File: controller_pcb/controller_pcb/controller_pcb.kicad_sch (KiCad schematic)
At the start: 2 parts

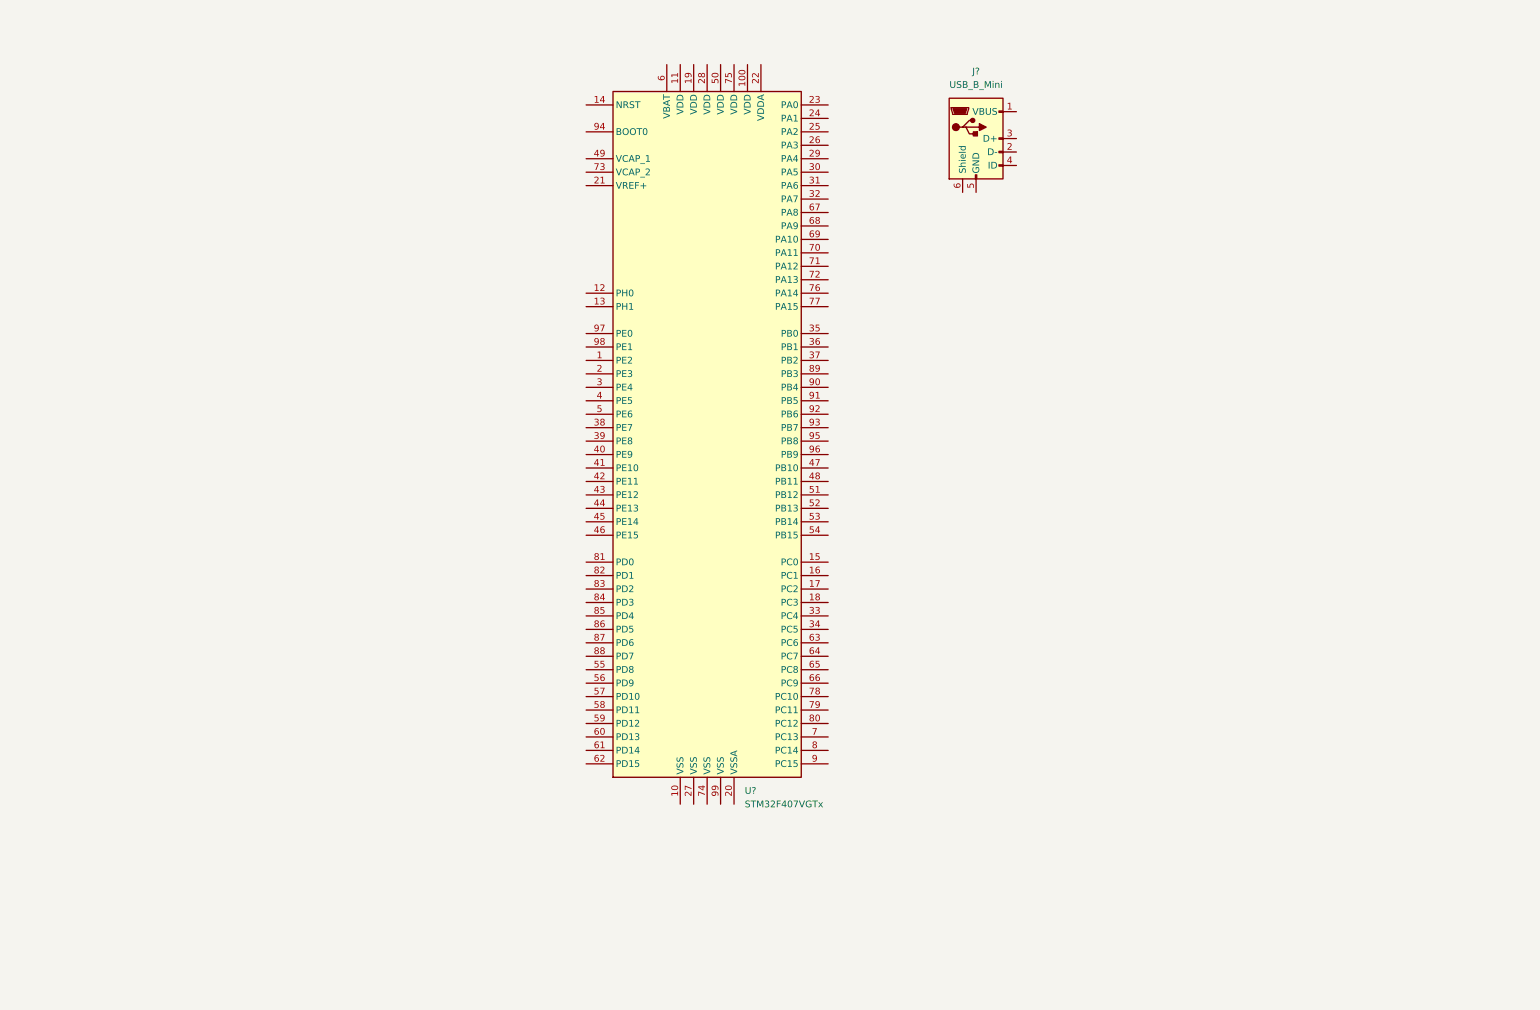
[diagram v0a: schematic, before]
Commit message: Added USB and SW Connector
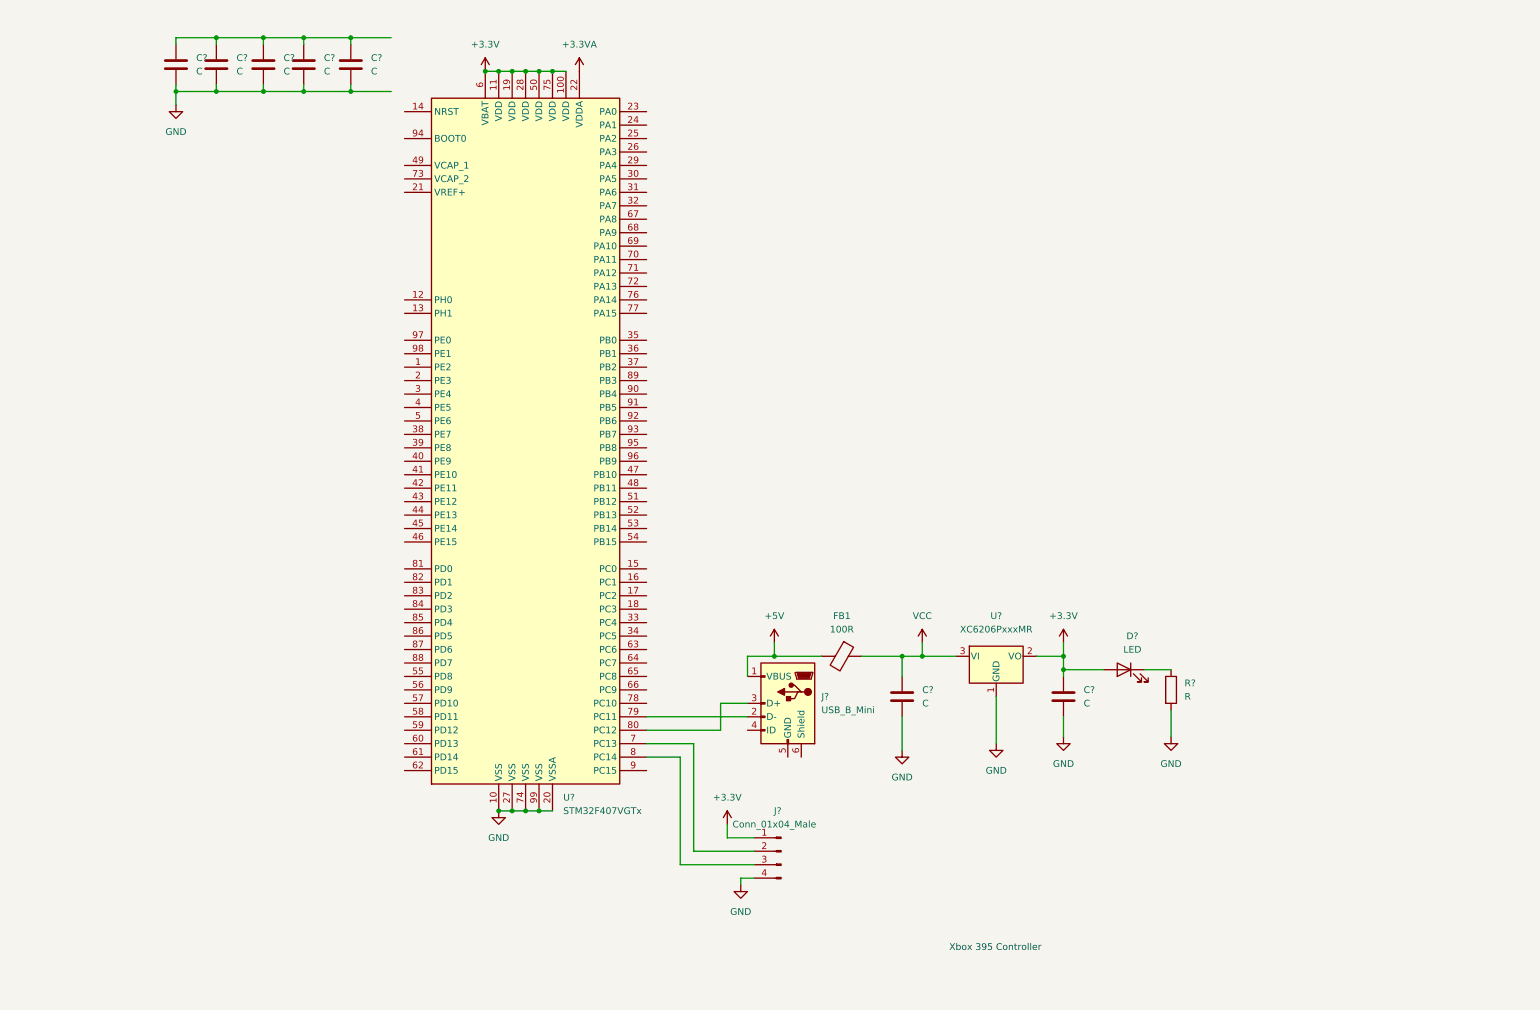
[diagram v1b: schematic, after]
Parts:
- added C? (x7): C, symbol Device:C
- added D?: LED, symbol Device:LED
- added FB1: 100R, symbol Device:FerriteBead
- added J?: Conn_01x04_Male, symbol Connector:Conn_01x04_Male
- added R?: R, symbol Device:R
- added U?: XC6206PxxxMR, Package_TO_SOT_SMD:SOT-23, symbol Regulator_Linear:XC6206PxxxMR
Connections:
- net GND: now reaches U?.10 (VSS)
- net GND: now also U?.20 (VSSA), U?.27 (VSS), U?.74 (VSS), U?.99 (VSS), C?.2, C?.2, C?.2, C?.2, C?.2, C?.2, C?.2, J?.4 (Pin_4), R?.2, U?.1 (GND)
- net +3V3: now reaches U?.100 (VDD)
- net +3V3: now also U?.11 (VDD), U?.19 (VDD), U?.28 (VDD), U?.50 (VDD), U?.6 (VBAT), U?.75 (VDD), C?.1, D?.2 (A), J?.1 (Pin_1), U?.2 (VO)
- net +3.3VA: now reaches U?.22 (VDDA)
- net at U?.7 (PC13): now also J?.2 (Pin_2)
- net at U?.79 (PC11): now also J?.2 (D-)
- net at U?.8 (PC14): now also J?.3 (Pin_3)
- net at U?.80 (PC12): now also J?.3 (D+)
- net +5V: now reaches J?.1 (VBUS)
- net +5V: now also FB1.2
- new net: D?.1 (K), R?.1
- new net: C?.1, C?.1, C?.1, C?.1, C?.1
- new net VCC: C?.1, FB1.1, U?.3 (VI)
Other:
- note added: "Xbox 395 Controller"
- moved on the sheet: J?, U?

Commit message: added one button
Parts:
- added SW?: SW_MEC_5E, symbol Switch:SW_MEC_5E
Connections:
- net GND: now also SW?.3 (K)
- net at U?.17 (PC2): now also SW?.2
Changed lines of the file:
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@@
+    (stroke (width 0) (type default) (color 0 0 0 0))
+  )
+  (wire (pts (xy 148.59 121.92) (xy 148.59 123.19))
     (stroke (width 0) (type default) (color 0 0 0 0))
   )
@@
     (stroke (width 0) (type default) (color 0 0 0 0))
   )
+  (wire (pts (xy 130.81 123.19) (xy 135.89 123.19))
+    (stroke (width 0) (type default) (color 0 0 0 0))
+  )
   (wire (pts (xy 58.42 27.94) (xy 66.04 27.94))
     (stroke (width 0) (type default) (color 0 0 0 0))
@@
     (stroke (width 0) (type default) (color 0 0 0 0))
   )
+  (wire (pts (xy 135.89 123.19) (xy 135.89 121.92))
+    (stroke (width 0) (type default) (color 0 0 0 0))
+  )
   (wire (pts (xy 179.07 134.62) (xy 182.88 134.62))
     (stroke (width 0) (type default) (color 0 0 0 0))
@@
   )
   (wire (pts (xy 58.42 17.78) (xy 66.04 17.78))
+    (stroke (width 0) (type default) (color 0 0 0 0))
+  )
+  (wire (pts (xy 146.05 121.92) (xy 148.59 121.92))
     (stroke (width 0) (type default) (color 0 0 0 0))
   )
@@
     (pin "1")
     (pin "2")
+  )
+  (symbol (lib_id "power:GND") (at 148.59 123.19 0) (unit 1)
+    (in_bom yes) (on_board yes) (fields_autoplaced)
+    (property "Reference" "#PWR?" (id 0) (at 148.59 129.54 0)
+      (effects (font (size 1.27 1.27)) hide)
+    )
+    (property "Value" "GND" (id 1) (at 148.59 128.27 0))
+    (property "Footprint" "" (id 2) (at 148.59 123.19 0)
+      (effects (font (size 1.27 1.27)) hide)
+    )
+    (property "Datasheet" "" (id 3) (at 148.59 123.19 0)
+      (effects (font (size 1.27 1.27)) hide)
+    )
+    (pin "1")
   )
   (symbol (lib_id "power:+3.3V") (at 100.33 24.13 0) (unit 1)
@@
     (pin "2")
   )
+  (symbol (lib_id "Switch:SW_MEC_5E") (at 140.97 121.92 0) (unit 1)
+    (in_bom yes) (on_board yes) (fields_autoplaced)
+    (property "Reference" "SW?" (id 0) (at 140.97 111.76 0))
+    (property "Value" "SW_MEC_5E" (id 1) (at 140.97 114.3 0))
+    (property "Footprint" "" (id 2) (at 140.97 114.3 0)
+      (effects (font (size 1.27 1.27)) hide)
+    )
+    (property "Datasheet" "http://www.apem.com/int/index.php?controller=attachment&id_attachment=1371" (id 3) (at 140.97 114.3 0)
+      (effects (font (size 1.27 1.27)) hide)
+    )
+    (pin "1")
+    (pin "2")
+    (pin "3")
+    (pin "4")
+  )
   (symbol (lib_id "power:GND") (at 148.59 177.8 0) (unit 1)
     (in_bom yes) (on_board yes) (fields_autoplaced)
@@
       (reference "#PWR?") (unit 1) (value "+3.3V") (footprint "")
     )
+    (path "/258bb5a8-c0f3-4b9a-b48a-8d07cffbd7e2"
+      (reference "#PWR?") (unit 1) (value "GND") (footprint "")
+    )
     (path "/261434a5-b86f-484c-94ef-3e941aaa290e"
       (reference "#PWR?") (unit 1) (value "+3.3V") (footprint "")
@@
       (reference "R?") (unit 1) (value "R") (footprint "")
     )
+    (path "/adaa39b1-4a83-435a-8ed8-680108ecec0f"
+      (reference "SW?") (unit 1) (value "SW_MEC_5E") (footprint "")
+    )
     (path "/3a1c998c-e2a1-4320-ae03-3251637afe67"

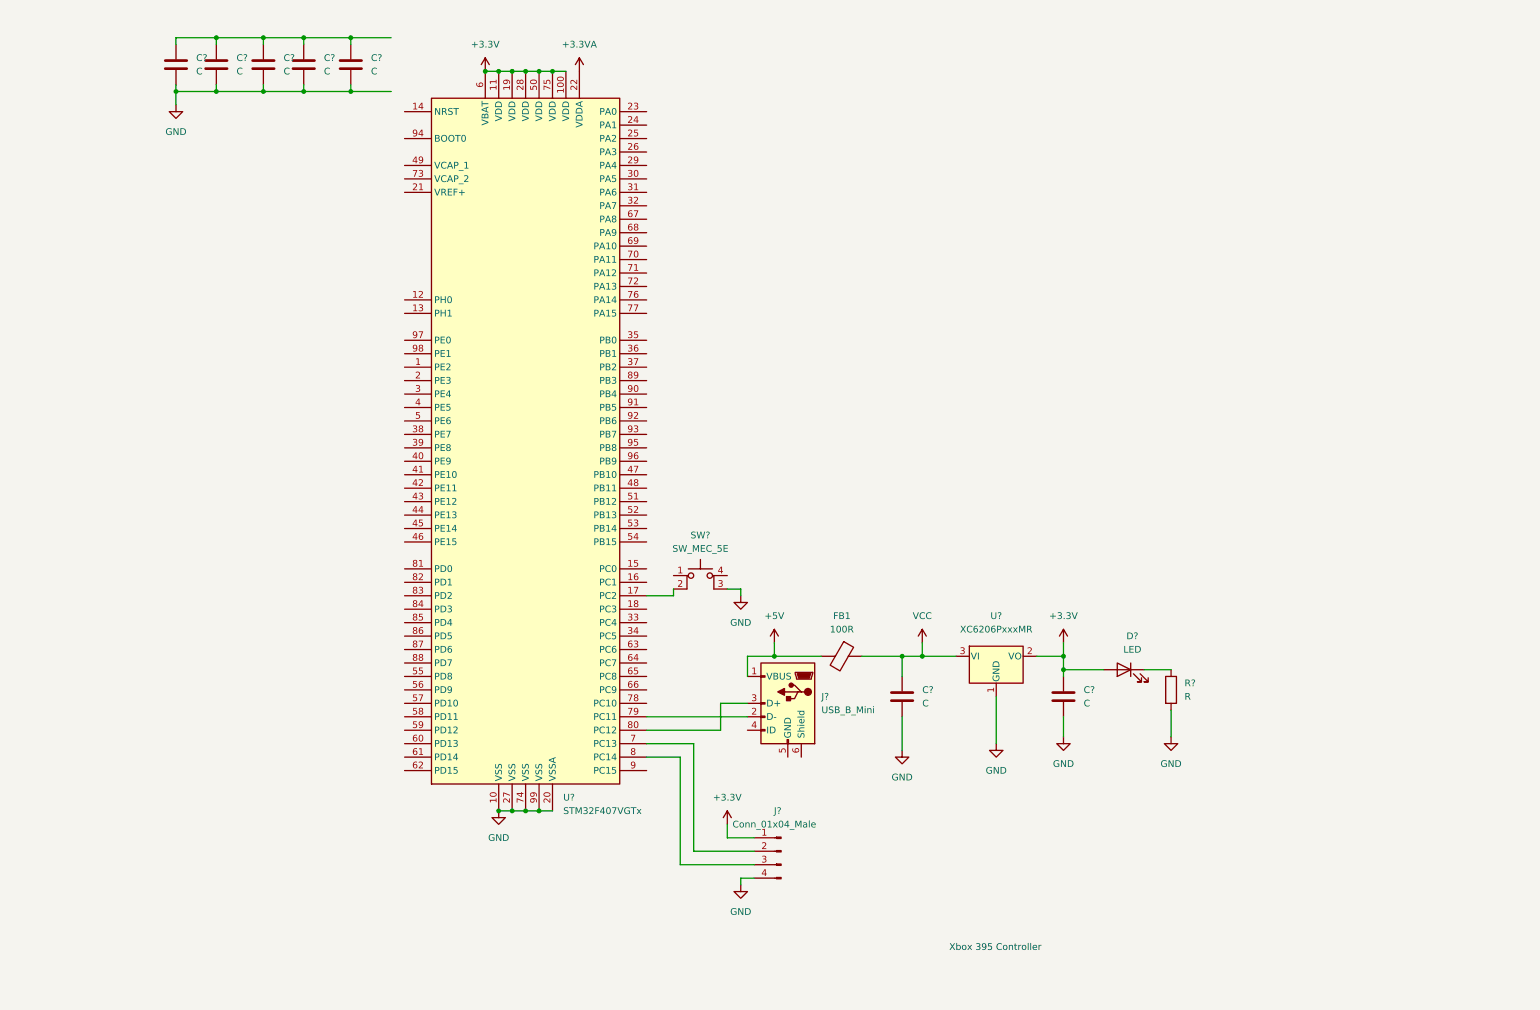
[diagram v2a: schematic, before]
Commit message: added all but one buttons
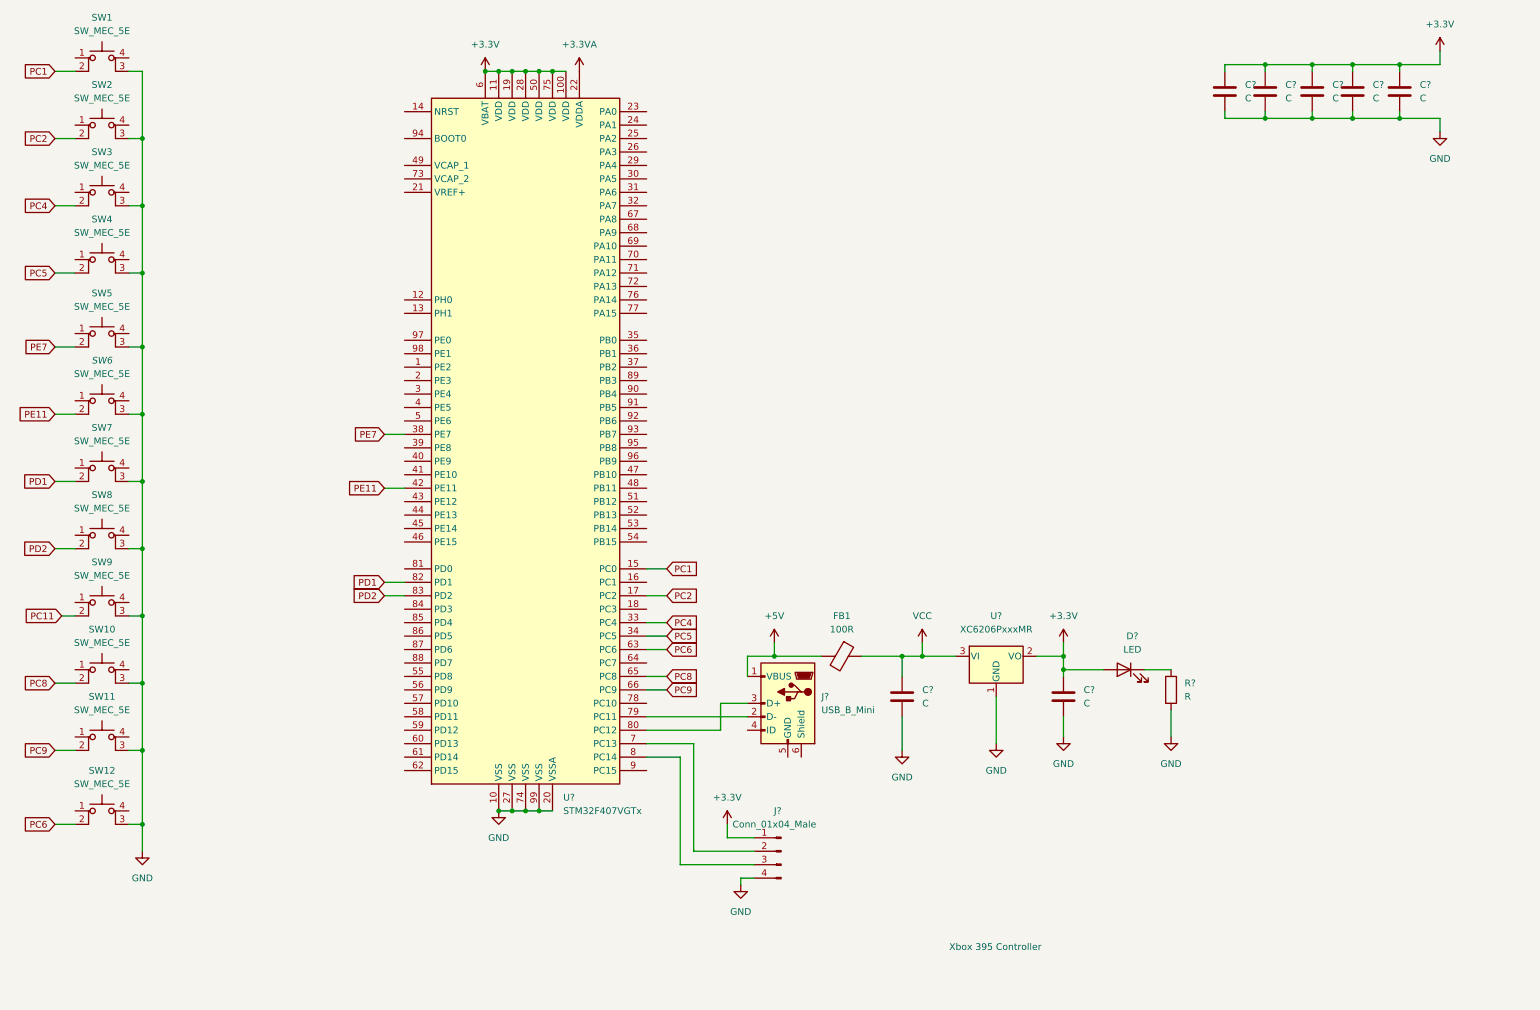
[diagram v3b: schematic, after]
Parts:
- added SW10, SW11, SW12, SW2, SW3, SW4, SW5, SW6, SW7, SW8, SW9: SW_MEC_5E, symbol Switch:SW_MEC_5E
- gave numbers to parts that had none: 1
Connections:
- net +3V3: now also C?.1, C?.1, C?.1, C?.1, C?.1
- net GND: now also SW10.3 (K), SW11.3 (K), SW12.3 (K), SW2.3 (K), SW3.3 (K), SW4.3 (K), SW5.3 (K), SW6.3 (K), SW7.3 (K), SW8.3 (K), SW9.3 (K)
- net PC1: now reaches U?.15 (PC0)
- net PC1: now also SW1.2
- net PC2: now reaches U?.17 (PC2)
- net PC2: now also SW2.2; no longer SW1.2
- net PC4: now reaches U?.33 (PC4)
- net PC4: now also SW3.2
- net PC5: now reaches U?.34 (PC5)
- net PC5: now also SW4.2
- net PE7: now reaches U?.38 (PE7)
- net PE7: now also SW5.2
- net PE11: now reaches U?.42 (PE11)
- net PE11: now also SW6.2
- net PC6: now reaches U?.63 (PC6)
- net PC6: now also SW12.2
- net PC8: now reaches U?.65 (PC8)
- net PC8: now also SW10.2
- net PC9: now reaches U?.66 (PC9)
- net PC9: now also SW11.2
- net PD1: now reaches U?.82 (PD1)
- net PD1: now also SW7.2
- net PD2: now reaches U?.83 (PD2)
- net PD2: now also SW8.2
- new net PC11: SW9.2
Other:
- moved on the sheet: C?, SW1

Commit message: changed port assignments
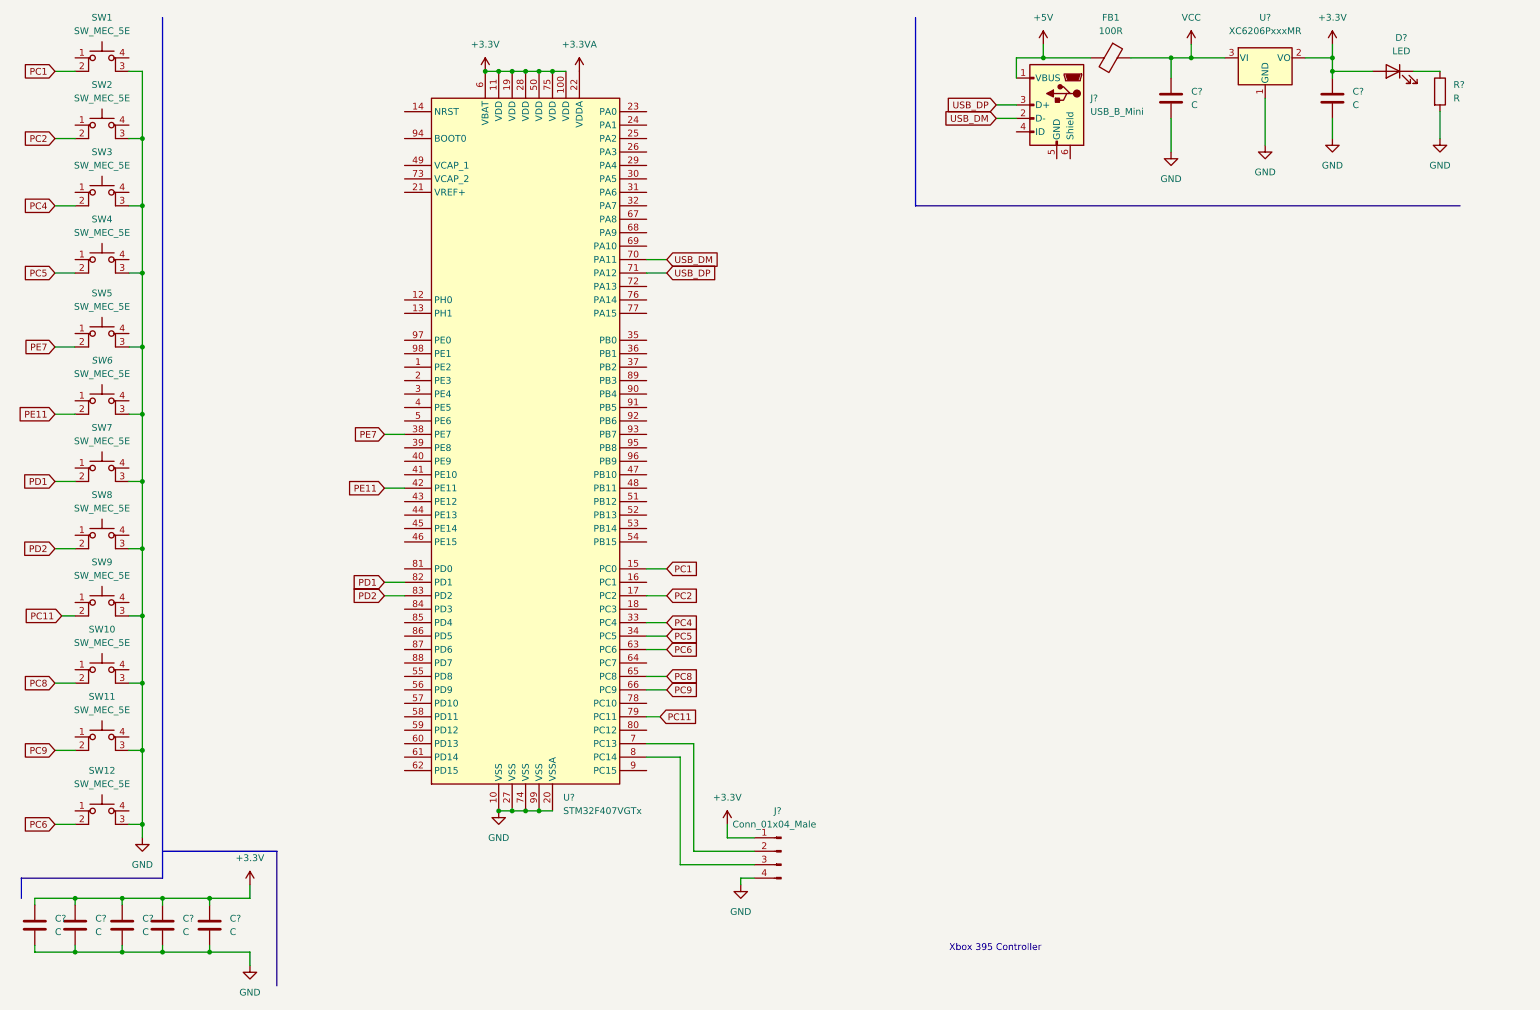
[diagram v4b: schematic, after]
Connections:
- net PC11: now also U?.79 (PC11)
- net USB_DM: now reaches U?.70 (PA11)
- net USB_DM: now also J?.2 (D-)
- net USB_DP: now reaches U?.71 (PA12)
- net USB_DP: now also J?.3 (D+)
- net at U?.80 (PC12): no longer J?.3 (D+)
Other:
- moved on the sheet: C?, D?, FB1, J?, R?, U?
